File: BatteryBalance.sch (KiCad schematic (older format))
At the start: 49 parts

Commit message: Think I just added labels?
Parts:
- gave numbers to parts that had none: 49

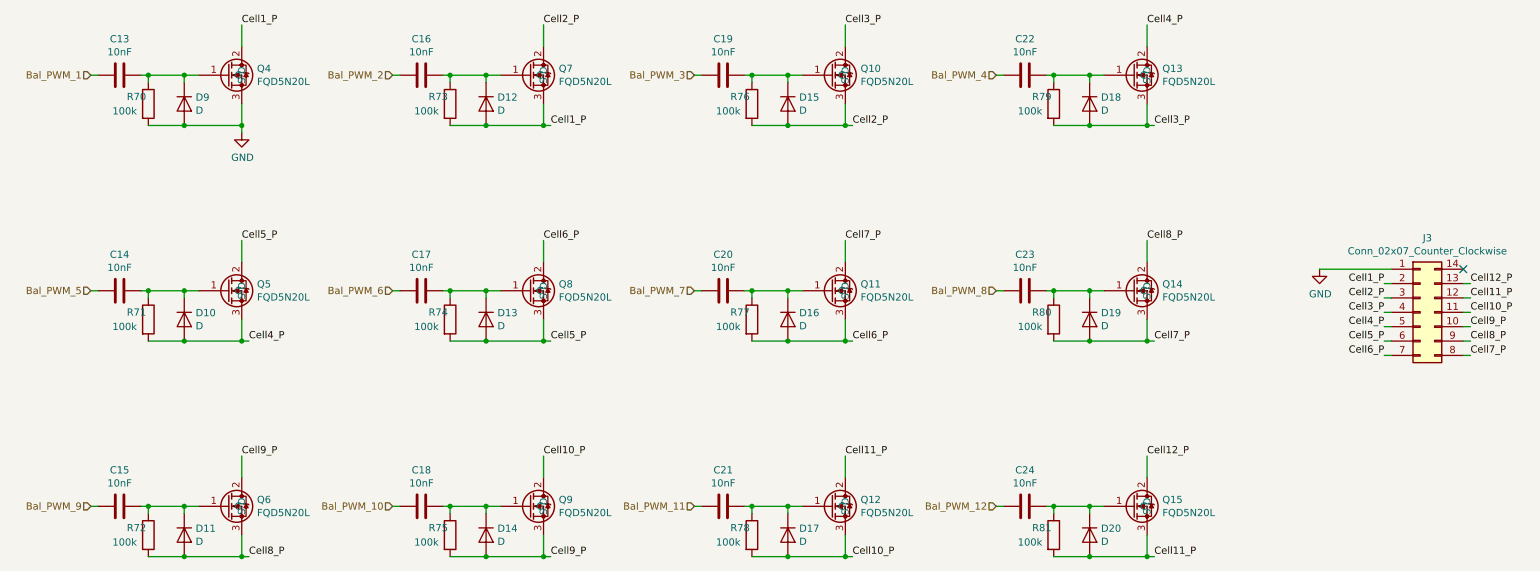
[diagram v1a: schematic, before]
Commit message: Added buttons + redid numbering
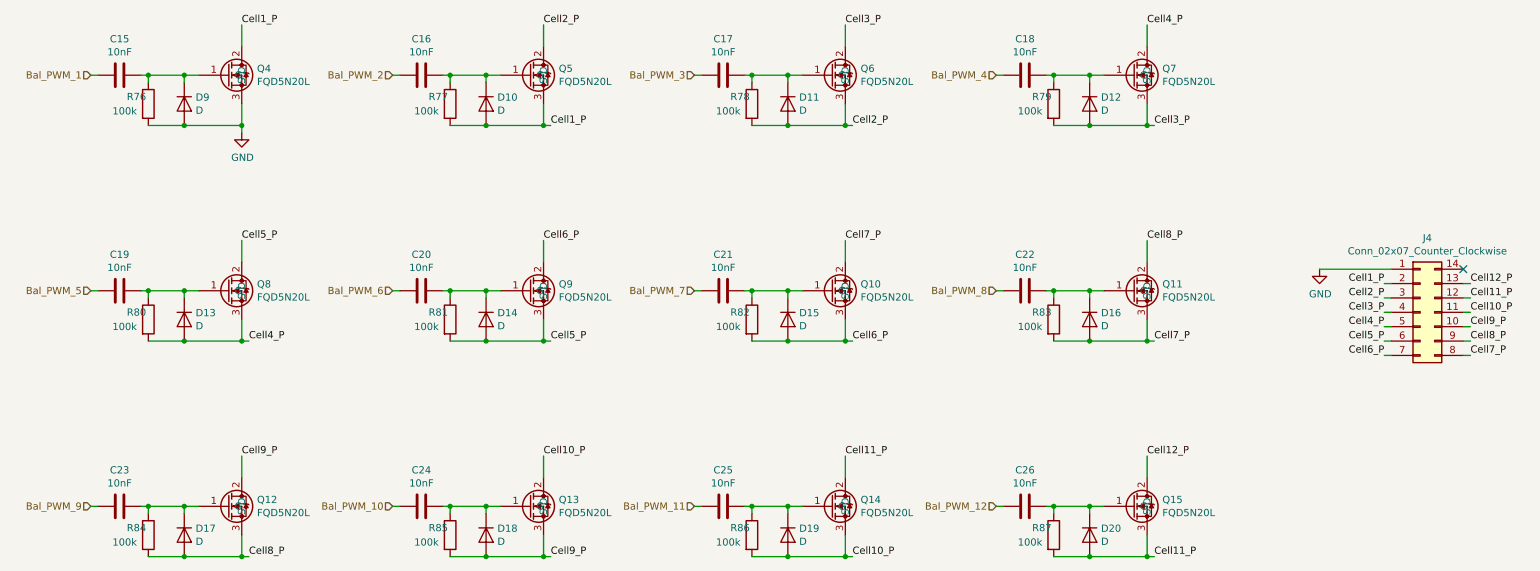
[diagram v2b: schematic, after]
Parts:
- renumbered C13 to C15, C19 to C17, C22 to C18, C14 to C19, C17 to C20, C20 to C21, C23 to C22, C15 to C23, C18 to C24, C21 to C25, C24 to C26, D12 to D10, D15 to D11, D18 to D12, D10 to D13, D13 to D14, D16 to D15, D19 to D16, D11 to D17, D14 to D18, D17 to D19, J3 to J4, Q11 to Q10, Q14 to Q11, Q6 to Q12, Q9 to Q13, Q12 to Q14, Q7 to Q5, Q10 to Q6, Q13 to Q7, Q5 to Q8, Q8 to Q9, R70 to R76, R73 to R77, R76 to R78, R71 to R80, R74 to R81, R77 to R82, R80 to R83, R72 to R84, R75 to R85, R78 to R86, R81 to R87

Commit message: Added most footprints
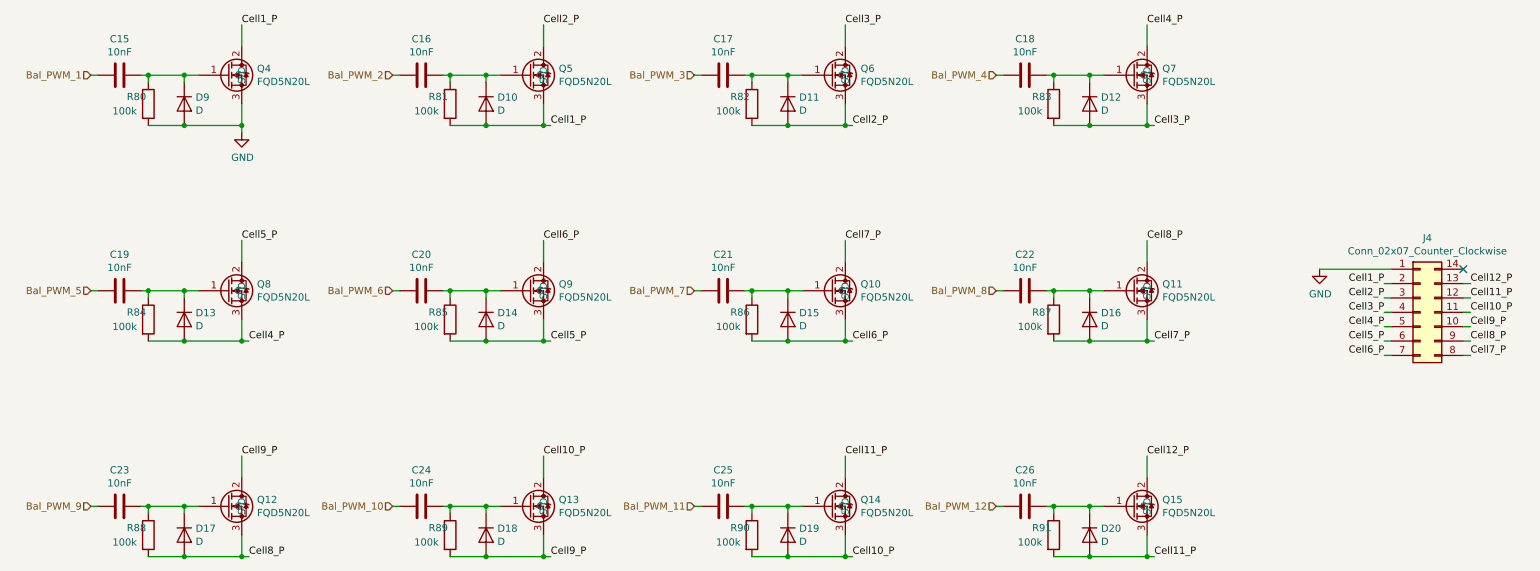
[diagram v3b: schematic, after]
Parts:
- C15, C16, C17, C18, C19, C20, C21, C22, C23, C24, C25, C26: footprint (none) -> Capacitor_SMD:C_1206_3216Metric
- D10, D11, D12, D13, D14, D15, D16, D17, D18, D19, D20, D9: footprint (none) -> Diode_SMD:D_0603_1608Metric_Pad1.05x0.95mm_HandSolder
- J4: footprint (none) -> Connector_PinHeader_2.54mm:PinHeader_2x07_P2.54mm_Vertical
- R80: renamed from R76; footprint (none) -> Resistor_SMD:R_0603_1608Metric_Pad1.05x0.95mm_HandSolder
- R81: renamed from R77; footprint (none) -> Resistor_SMD:R_0603_1608Metric_Pad1.05x0.95mm_HandSolder
- R82: renamed from R78; footprint (none) -> Resistor_SMD:R_0603_1608Metric_Pad1.05x0.95mm_HandSolder
- R83: renamed from R79; footprint (none) -> Resistor_SMD:R_0603_1608Metric_Pad1.05x0.95mm_HandSolder
- R84: renamed from R80; footprint (none) -> Resistor_SMD:R_0603_1608Metric_Pad1.05x0.95mm_HandSolder
- R85: renamed from R81; footprint (none) -> Resistor_SMD:R_0603_1608Metric_Pad1.05x0.95mm_HandSolder
- R86: renamed from R82; footprint (none) -> Resistor_SMD:R_0603_1608Metric_Pad1.05x0.95mm_HandSolder
- R87: renamed from R83; footprint (none) -> Resistor_SMD:R_0603_1608Metric_Pad1.05x0.95mm_HandSolder
- R88: renamed from R84; footprint (none) -> Resistor_SMD:R_0603_1608Metric_Pad1.05x0.95mm_HandSolder
- R89: renamed from R85; footprint (none) -> Resistor_SMD:R_0603_1608Metric_Pad1.05x0.95mm_HandSolder
- R90: renamed from R86; footprint (none) -> Resistor_SMD:R_0603_1608Metric_Pad1.05x0.95mm_HandSolder
- R91: renamed from R87; footprint (none) -> Resistor_SMD:R_0603_1608Metric_Pad1.05x0.95mm_HandSolder

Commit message: Switched to lower GPIO pin part to save space
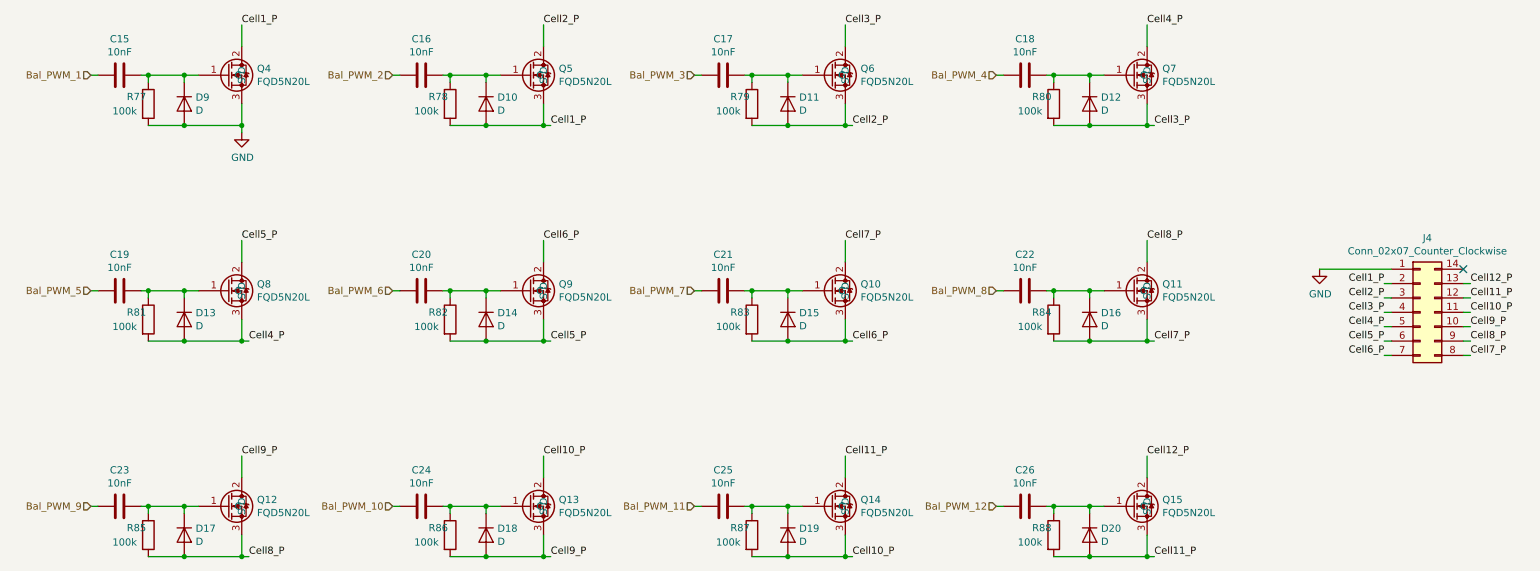
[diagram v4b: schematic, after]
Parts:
- renumbered R80 to R77, R81 to R78, R82 to R79, R83 to R80, R84 to R81, R85 to R82, R86 to R83, R87 to R84, R88 to R85, R89 to R86, R90 to R87, R91 to R88
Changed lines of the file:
@@
 P 9650 2850
 AR Path="/5F70A721/5F78CA1C" Ref="#PWR?"  Part="1"
-AR Path="/5F7870B7/5F78CA1C" Ref="#PWR088"  Part="1"
-F 0 "#PWR088" H 9650 2600 50  0001 C CNN
+AR Path="/5F7870B7/5F78CA1C" Ref="#PWR087"  Part="1"
+F 0 "#PWR087" H 9650 2600 50  0001 C CNN
 F 1 "GND" H 9655 2677 50  0000 C CNN
 F 2 "" H 9650 2850 50  0001 C CNN
@@
 $EndComp
 $Comp
-L Device:R R80
+L Device:R R77
 U 1 1 5F79167A
 P 1500 1700
-F 0 "R80" H 1350 1750 50  0000 L CNN
+F 0 "R77" H 1350 1750 50  0000 L CNN
 F 1 "100k" H 1250 1650 50  0000 L CNN
 F 2 "Resistor_SMD:R_0603_1608Metric_Pad1.05x0.95mm_HandSolder" V 1430 1700 50  0001 C CNN
@@
 P 2150 1900
 AR Path="/5F70A721/5F793673" Ref="#PWR?"  Part="1"
-AR Path="/5F7870B7/5F793673" Ref="#PWR087"  Part="1"
-F 0 "#PWR087" H 2150 1650 50  0001 C CNN
+AR Path="/5F7870B7/5F793673" Ref="#PWR086"  Part="1"
+F 0 "#PWR086" H 2150 1650 50  0001 C CNN
 F 1 "GND" H 2155 1727 50  0000 C CNN
 F 2 "" H 2150 1900 50  0001 C CNN
@@
 $EndComp
 $Comp
-L Device:R R81
+L Device:R R78
 U 1 1 5F796EF2
 P 3600 1700
-F 0 "R81" H 3450 1750 50  0000 L CNN
+F 0 "R78" H 3450 1750 50  0000 L CNN
 F 1 "100k" H 3350 1650 50  0000 L CNN
 F 2 "Resistor_SMD:R_0603_1608Metric_Pad1.05x0.95mm_HandSolder" V 3530 1700 50  0001 C CNN
@@
 $EndComp
 $Comp
-L Device:R R82
+L Device:R R79
 U 1 1 5F79E65B
 P 5700 1700
-F 0 "R82" H 5550 1750 50  0000 L CNN
+F 0 "R79" H 5550 1750 50  0000 L CNN
 F 1 "100k" H 5450 1650 50  0000 L CNN
 F 2 "Resistor_SMD:R_0603_1608Metric_Pad1.05x0.95mm_HandSolder" V 5630 1700 50  0001 C CNN
@@
 $EndComp
 $Comp
-L Device:R R83
+L Device:R R80
 U 1 1 5F7A2D3B
 P 7800 1700
-F 0 "R83" H 7650 1750 50  0000 L CNN
+F 0 "R80" H 7650 1750 50  0000 L CNN
 F 1 "100k" H 7550 1650 50  0000 L CNN
 F 2 "Resistor_SMD:R_0603_1608Metric_Pad1.05x0.95mm_HandSolder" V 7730 1700 50  0001 C CNN
@@
 $EndComp
 $Comp
-L Device:R R84
+L Device:R R81
 U 1 1 5F7ADC95
 P 1500 3200
-F 0 "R84" H 1350 3250 50  0000 L CNN
+F 0 "R81" H 1350 3250 50  0000 L CNN
 F 1 "100k" H 1250 3150 50  0000 L CNN
 F 2 "Resistor_SMD:R_0603_1608Metric_Pad1.05x0.95mm_HandSolder" V 1430 3200 50  0001 C CNN
@@
 $EndComp
 $Comp
-L Device:R R85
+L Device:R R82
 U 1 1 5F7ADCC2
 P 3600 3200
-F 0 "R85" H 3450 3250 50  0000 L CNN
+F 0 "R82" H 3450 3250 50  0000 L CNN
 F 1 "100k" H 3350 3150 50  0000 L CNN
 F 2 "Resistor_SMD:R_0603_1608Metric_Pad1.05x0.95mm_HandSolder" V 3530 3200 50  0001 C CNN
@@
 $EndComp
 $Comp
-L Device:R R86
+L Device:R R83
 U 1 1 5F7ADCEF
 P 5700 3200
-F 0 "R86" H 5550 3250 50  0000 L CNN
+F 0 "R83" H 5550 3250 50  0000 L CNN
 F 1 "100k" H 5450 3150 50  0000 L CNN
 F 2 "Resistor_SMD:R_0603_1608Metric_Pad1.05x0.95mm_HandSolder" V 5630 3200 50  0001 C CNN
@@
 $EndComp
 $Comp
-L Device:R R87
+L Device:R R84
 U 1 1 5F7ADD1C
 P 7800 3200
-F 0 "R87" H 7650 3250 50  0000 L CNN
+F 0 "R84" H 7650 3250 50  0000 L CNN
 F 1 "100k" H 7550 3150 50  0000 L CNN
 F 2 "Resistor_SMD:R_0603_1608Metric_Pad1.05x0.95mm_HandSolder" V 7730 3200 50  0001 C CNN
@@
 $EndComp
 $Comp
-L Device:R R88
+L Device:R R85
 U 1 1 5F7BAE2E
 P 1500 4700
-F 0 "R88" H 1350 4750 50  0000 L CNN
+F 0 "R85" H 1350 4750 50  0000 L CNN
 F 1 "100k" H 1250 4650 50  0000 L CNN
 F 2 "Resistor_SMD:R_0603_1608Metric_Pad1.05x0.95mm_HandSolder" V 1430 4700 50  0001 C CNN
@@
 $EndComp
 $Comp
-L Device:R R89
+L Device:R R86
 U 1 1 5F7BAE5B
 P 3600 4700
-F 0 "R89" H 3450 4750 50  0000 L CNN
+F 0 "R86" H 3450 4750 50  0000 L CNN
 F 1 "100k" H 3350 4650 50  0000 L CNN
 F 2 "Resistor_SMD:R_0603_1608Metric_Pad1.05x0.95mm_HandSolder" V 3530 4700 50  0001 C CNN
@@
 $EndComp
 $Comp
-L Device:R R90
+L Device:R R87
 U 1 1 5F7BAE88
 P 5700 4700
-F 0 "R90" H 5550 4750 50  0000 L CNN
+F 0 "R87" H 5550 4750 50  0000 L CNN
 F 1 "100k" H 5450 4650 50  0000 L CNN
 F 2 "Resistor_SMD:R_0603_1608Metric_Pad1.05x0.95mm_HandSolder" V 5630 4700 50  0001 C CNN
@@
 $EndComp
 $Comp
-L Device:R R91
+L Device:R R88
 U 1 1 5F7BAEB5
 P 7800 4700
-F 0 "R91" H 7650 4750 50  0000 L CNN
+F 0 "R88" H 7650 4750 50  0000 L CNN
 F 1 "100k" H 7550 4650 50  0000 L CNN
 F 2 "Resistor_SMD:R_0603_1608Metric_Pad1.05x0.95mm_HandSolder" V 7730 4700 50  0001 C CNN

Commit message: Removed SD card Adapter, added programming port
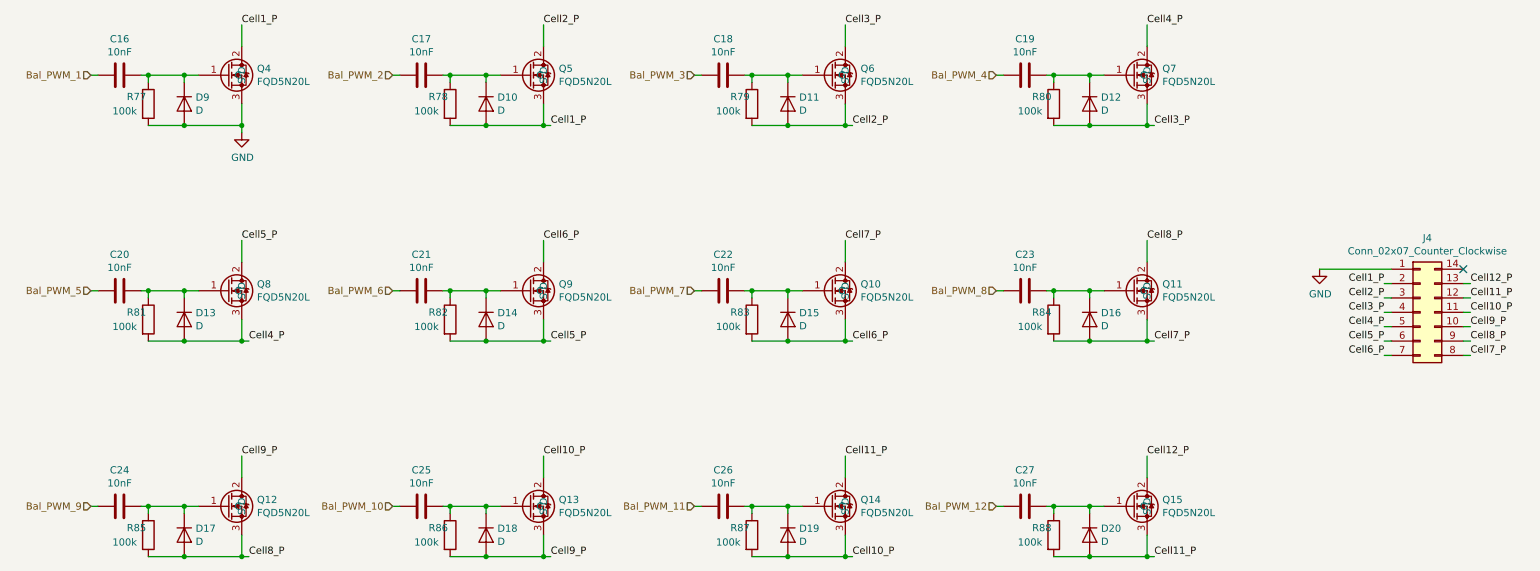
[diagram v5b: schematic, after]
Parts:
- renumbered C15 to C16, C16 to C17, C17 to C18, C18 to C19, C19 to C20, C20 to C21, C21 to C22, C22 to C23, C23 to C24, C24 to C25, C25 to C26, C26 to C27
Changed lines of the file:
@@
 NoConn ~ 10650 2850
 $Comp
-L Device:C C15
+L Device:C C16
 U 1 1 5F78D337
 P 1300 1500
-F 0 "C15" V 1048 1500 50  0000 C CNN
+F 0 "C16" V 1048 1500 50  0000 C CNN
 F 1 "10nF" V 1139 1500 50  0000 C CNN
 F 2 "Capacitor_SMD:C_1206_3216Metric" H 1338 1350 50  0001 C CNN
@@
 Connection ~ 2150 1850
 $Comp
-L Device:C C16
+L Device:C C17
 U 1 1 5F796EE6
 P 3400 1500
-F 0 "C16" V 3148 1500 50  0000 C CNN
+F 0 "C17" V 3148 1500 50  0000 C CNN
 F 1 "10nF" V 3239 1500 50  0000 C CNN
 F 2 "Capacitor_SMD:C_1206_3216Metric" H 3438 1350 50  0001 C CNN
@@
 	4250 1300 4250 1150
 $Comp
-L Device:C C17
+L Device:C C18
 U 1 1 5F79E64F
 P 5500 1500
-F 0 "C17" V 5248 1500 50  0000 C CNN
+F 0 "C18" V 5248 1500 50  0000 C CNN
 F 1 "10nF" V 5339 1500 50  0000 C CNN
 F 2 "Capacitor_SMD:C_1206_3216Metric" H 5538 1350 50  0001 C CNN
@@
 	6350 1300 6350 1150
 $Comp
-L Device:C C18
+L Device:C C19
 U 1 1 5F7A2D2F
 P 7600 1500
-F 0 "C18" V 7348 1500 50  0000 C CNN
+F 0 "C19" V 7348 1500 50  0000 C CNN
 F 1 "10nF" V 7439 1500 50  0000 C CNN
 F 2 "Capacitor_SMD:C_1206_3216Metric" H 7638 1350 50  0001 C CNN
@@
 	8450 1300 8450 1150
 $Comp
-L Device:C C19
+L Device:C C20
 U 1 1 5F7ADC89
 P 1300 3000
-F 0 "C19" V 1048 3000 50  0000 C CNN
+F 0 "C20" V 1048 3000 50  0000 C CNN
 F 1 "10nF" V 1139 3000 50  0000 C CNN
 F 2 "Capacitor_SMD:C_1206_3216Metric" H 1338 2850 50  0001 C CNN
@@
 	2150 2800 2150 2650
 $Comp
-L Device:C C20
+L Device:C C21
 U 1 1 5F7ADCB6
 P 3400 3000
-F 0 "C20" V 3148 3000 50  0000 C CNN
+F 0 "C21" V 3148 3000 50  0000 C CNN
 F 1 "10nF" V 3239 3000 50  0000 C CNN
 F 2 "Capacitor_SMD:C_1206_3216Metric" H 3438 2850 50  0001 C CNN
@@
 	4250 2800 4250 2650
 $Comp
-L Device:C C21
+L Device:C C22
 U 1 1 5F7ADCE3
 P 5500 3000
-F 0 "C21" V 5248 3000 50  0000 C CNN
+F 0 "C22" V 5248 3000 50  0000 C CNN
 F 1 "10nF" V 5339 3000 50  0000 C CNN
 F 2 "Capacitor_SMD:C_1206_3216Metric" H 5538 2850 50  0001 C CNN
@@
 	6350 2800 6350 2650
 $Comp
-L Device:C C22
+L Device:C C23
 U 1 1 5F7ADD10
 P 7600 3000
-F 0 "C22" V 7348 3000 50  0000 C CNN
+F 0 "C23" V 7348 3000 50  0000 C CNN
 F 1 "10nF" V 7439 3000 50  0000 C CNN
 F 2 "Capacitor_SMD:C_1206_3216Metric" H 7638 2850 50  0001 C CNN
@@
 	8450 2800 8450 2650
 $Comp
-L Device:C C23
+L Device:C C24
 U 1 1 5F7BAE22
 P 1300 4500
-F 0 "C23" V 1048 4500 50  0000 C CNN
+F 0 "C24" V 1048 4500 50  0000 C CNN
 F 1 "10nF" V 1139 4500 50  0000 C CNN
 F 2 "Capacitor_SMD:C_1206_3216Metric" H 1338 4350 50  0001 C CNN
@@
 	2150 4300 2150 4150
 $Comp
-L Device:C C24
+L Device:C C25
 U 1 1 5F7BAE4F
 P 3400 4500
-F 0 "C24" V 3148 4500 50  0000 C CNN
+F 0 "C25" V 3148 4500 50  0000 C CNN
 F 1 "10nF" V 3239 4500 50  0000 C CNN
 F 2 "Capacitor_SMD:C_1206_3216Metric" H 3438 4350 50  0001 C CNN
@@
 	4250 4300 4250 4150
 $Comp
-L Device:C C25
+L Device:C C26
 U 1 1 5F7BAE7C
 P 5500 4500
-F 0 "C25" V 5248 4500 50  0000 C CNN
+F 0 "C26" V 5248 4500 50  0000 C CNN
 F 1 "10nF" V 5339 4500 50  0000 C CNN
 F 2 "Capacitor_SMD:C_1206_3216Metric" H 5538 4350 50  0001 C CNN
@@
 	6350 4300 6350 4150
 $Comp
-L Device:C C26
+L Device:C C27
 U 1 1 5F7BAEA9
 P 7600 4500
-F 0 "C26" V 7348 4500 50  0000 C CNN
+F 0 "C27" V 7348 4500 50  0000 C CNN
 F 1 "10nF" V 7439 4500 50  0000 C CNN
 F 2 "Capacitor_SMD:C_1206_3216Metric" H 7638 4350 50  0001 C CNN

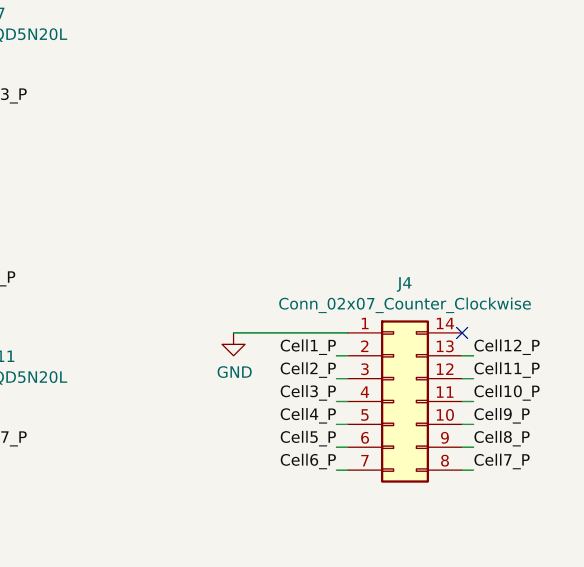
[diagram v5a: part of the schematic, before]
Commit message: Added ext ADC pin and fixed connection bugs
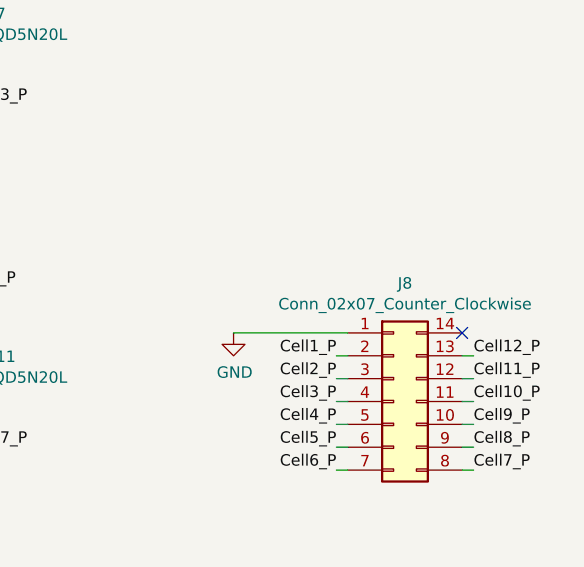
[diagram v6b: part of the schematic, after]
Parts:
- renumbered J4 to J8
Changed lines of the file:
@@
 P 9650 2850
 AR Path="/5F70A721/5F78CA1C" Ref="#PWR?"  Part="1"
-AR Path="/5F7870B7/5F78CA1C" Ref="#PWR087"  Part="1"
-F 0 "#PWR087" H 9650 2600 50  0001 C CNN
+AR Path="/5F7870B7/5F78CA1C" Ref="#PWR089"  Part="1"
+F 0 "#PWR089" H 9650 2600 50  0001 C CNN
 F 1 "GND" H 9655 2677 50  0000 C CNN
 F 2 "" H 9650 2850 50  0001 C CNN
@@
 Cell6_P
 $Comp
-L Connector_Generic:Conn_02x07_Counter_Clockwise J4
+L Connector_Generic:Conn_02x07_Counter_Clockwise J8
 U 1 1 5F78CA28
 P 10350 3150
-F 0 "J4" H 10400 3667 50  0000 C CNN
+F 0 "J8" H 10400 3667 50  0000 C CNN
 F 1 "Conn_02x07_Counter_Clockwise" H 10400 3576 50  0000 C CNN
 F 2 "Connector_PinHeader_2.54mm:PinHeader_2x07_P2.54mm_Vertical" H 10350 3150 50  0001 C CNN
@@
 P 2150 1900
 AR Path="/5F70A721/5F793673" Ref="#PWR?"  Part="1"
-AR Path="/5F7870B7/5F793673" Ref="#PWR086"  Part="1"
-F 0 "#PWR086" H 2150 1650 50  0001 C CNN
+AR Path="/5F7870B7/5F793673" Ref="#PWR088"  Part="1"
+F 0 "#PWR088" H 2150 1650 50  0001 C CNN
 F 1 "GND" H 2155 1727 50  0000 C CNN
 F 2 "" H 2150 1900 50  0001 C CNN
